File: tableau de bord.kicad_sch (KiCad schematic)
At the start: 19 parts, among them J2 Alim, SW1 LVMS, SW2 TS, SW3 R2D, SW4 TS OFF, SW5 SW_Push, U1 L7805

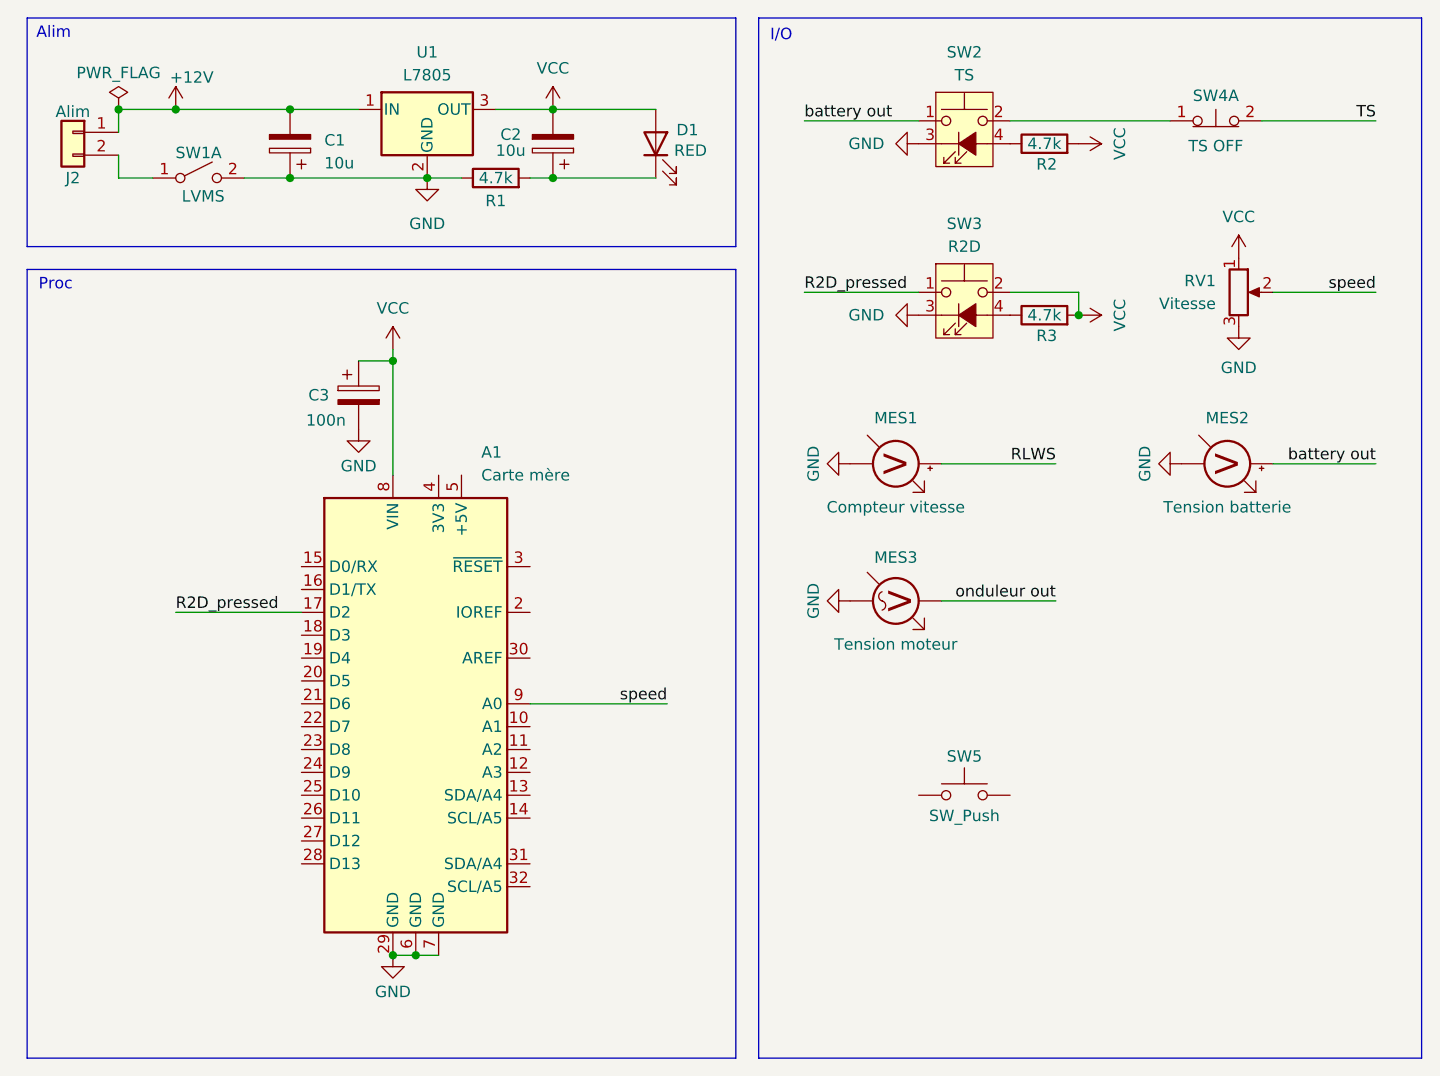
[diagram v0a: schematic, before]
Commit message: Ajout des boutons I/O pour les scénario et pannes
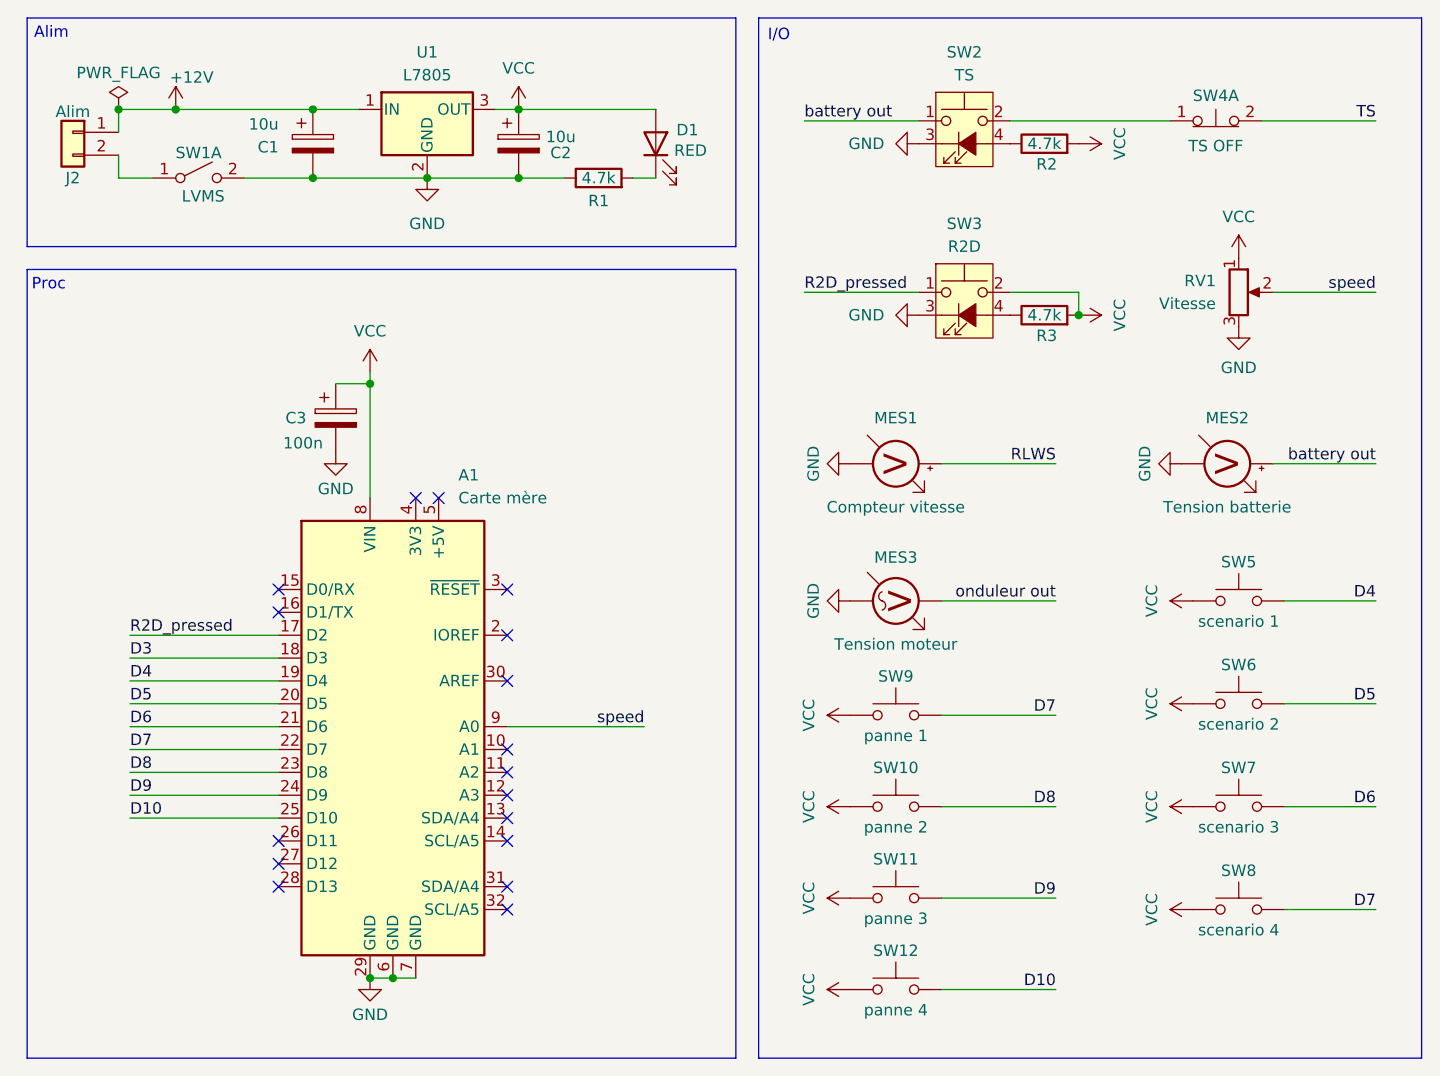
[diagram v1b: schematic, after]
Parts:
- added SW10: panne 2, symbol Switch:SW_Push
- added SW11: panne 3, symbol Switch:SW_Push
- added SW12: panne 4, symbol Switch:SW_Push
- added SW6: scenario 2, symbol Switch:SW_Push
- added SW7: scenario 3, symbol Switch:SW_Push
- added SW8: scenario 4, symbol Switch:SW_Push
- added SW9: panne 1, symbol Switch:SW_Push
- SW5: value SW_Push -> scenario 1
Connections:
- net +12V: now also C1.1; no longer C1.2
- net GND: now also C1.2, C2.2; no longer C1.1
- net VCC: now also C2.1, SW5.1, SW10.1, SW11.1, SW12.1, SW6.1, SW7.1, SW8.1, SW9.1; no longer C2.2
- net at D1.1 (K), R1.2: no longer C2.1
- net D3: now reaches A1.18 (D3)
- net D4: now reaches A1.19 (D4)
- net D4: now also SW5.2
- net D5: now reaches A1.20 (D5)
- net D5: now also SW6.2
- net D6: now reaches A1.21 (D6)
- net D6: now also SW7.2
- net D7: now reaches A1.22 (D7)
- net D7: now also SW8.2, SW9.2
- net D8: now reaches A1.23 (D8)
- net D8: now also SW10.2
- net D9: now reaches A1.24 (D9)
- net D9: now also SW11.2
- net D10: now reaches A1.25 (D10)
- net D10: now also SW12.2
- no-connect marks 0 -> 17
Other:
- moved on the sheet: A1, C1, C2, C3, SW5

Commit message: Retirer le voltmètre
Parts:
- removed MES1: Compteur vitesse, symbol Device:Voltmeter_DC
- removed MES2: Tension batterie, symbol Device:Voltmeter_DC
- removed MES3: Tension moteur, symbol Device:Voltmeter_AC
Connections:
- net D3: no longer names the net of A1.18 (D3)
- net battery out renamed +60V
- no-connect marks 17 -> 18
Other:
- moved on the sheet: SW10, SW11, SW12, SW5, SW6, SW7, SW8, SW9

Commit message: version prête pour révision
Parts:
- removed SW1: LVMS, symbol Switch:SW_DPST_x2
- removed SW4: TS OFF, symbol Switch:SW_Push_Open_Dual_x2
- added J1: Connecteur voiture, symbol Connector:Conn_01x02_Pin
- added SW1: LVMS, symbol Switch:SW_SPST
- added SW4: TSMS, symbol Switch:SW_Push_Open
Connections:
- net GND: now also SW1.2 (B)
- net TS: now also SW4.2 (B)
- net at A1.15 (D0/RX): now also J1.1 (Pin_1)
- net at A1.16 (D1/TX): now also J1.2 (Pin_2)
- net at SW2.2: now also SW4.1 (A)
- net at J2.2 (Pin_2): now also SW1.1 (A)
- no-connect marks 18 -> 16
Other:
- title: (none) -> Carte du tableu de bord

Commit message: Ajout de résistances pull up
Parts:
- removed SW8: scenario 4, symbol Switch:SW_Push
- added R10, R4, R5, R6, R7, R8, R9: 10k, symbol Device:R
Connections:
- net D10: now also R7.1
- net D4: now also R8.1
- net D5: now also R9.1
- net D6: now also R10.1
- net D7: now also R4.1
- net D8: now also R5.1
- net D9: now also R6.1
- net GND: now also SW10.1, SW11.1, SW12.1, SW5.1, SW6.1, SW7.1, SW9.1
- net VCC: now also R10.2, R4.2, R5.2, R6.2, R7.2, R8.2, R9.2; no longer SW10.1, SW11.1, SW12.1, SW5.1, SW6.1, SW7.1, SW9.1
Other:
- moved on the sheet: SW9

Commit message: Version 1
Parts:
- removed A1: Carte mère, Module:Arduino_UNO_R3, symbol MCU_Module:Arduino_UNO_R3
- removed C3: 100n, symbol Device:C_Polarized
- removed D1: RED, symbol Device:LED
- removed J1: Connecteur voiture, symbol Connector:Conn_01x02_Pin
- removed R1: 4.7k, symbol Device:R
- removed R10, R8, R9: 10k, symbol Device:R
- removed RV1: Vitesse, symbol Device:R_Potentiometer
- removed SW1: LVMS, symbol Switch:SW_SPST
- removed SW10: panne 2, symbol Switch:SW_Push
- removed SW11: panne 3, symbol Switch:SW_Push
- removed SW12: panne 4, symbol Switch:SW_Push
- removed SW2: TS, symbol Switch:SW_Push_LED
- removed SW3: R2D, symbol Switch:SW_Push_LED
- removed SW4: TSMS, symbol Switch:SW_Push_Open
- removed SW5: scenario 1, symbol Switch:SW_Push
- removed SW6: scenario 2, symbol Switch:SW_Push
- removed SW7: scenario 3, symbol Switch:SW_Push
- removed SW9: panne 1, symbol Switch:SW_Push
- added A2: Arduino_Nano_ESP32, Module:Arduino_Nano, symbol MCU_Module:Arduino_Nano_ESP32
- added J1: TS ON, Connector_PinSocket_2.00mm:PinSocket_1x03_P2.00mm_Vertical, symbol Connector:Conn_01x03_Socket
- added J3: R2D, Connector_PinSocket_2.00mm:PinSocket_1x03_P2.00mm_Vertical, symbol Connector:Conn_01x03_Socket
- added J4: Potentiometre, Connector_PinSocket_2.00mm:PinSocket_1x03_P2.00mm_Vertical, symbol Connector:Conn_01x03_Socket
- added J5: commande onduleur, Connector_PinSocket_2.00mm:PinSocket_1x02_P2.00mm_Vertical, symbol Connector:Conn_01x02_Socket
- C1, C2: footprint (none) -> Capacitor_THT:CP_Radial_D8.0mm_P5.00mm
- J2: footprint (none) -> Connector_PinSocket_2.00mm:PinSocket_1x02_P2.00mm_Vertical
- R2: footprint (none) -> Resistor_THT:R_Axial_DIN0204_L3.6mm_D1.6mm_P1.90mm_Vertical
- R3: value 4.7k -> 47k; footprint (none) -> Resistor_THT:R_Axial_DIN0204_L3.6mm_D1.6mm_P1.90mm_Vertical
- R4, R6, R7: value 10k -> 4.7k; footprint (none) -> Resistor_THT:R_Axial_DIN0204_L3.6mm_D1.6mm_P1.90mm_Vertical
- R5: value 10k -> 47k; footprint (none) -> Resistor_THT:R_Axial_DIN0204_L3.6mm_D1.6mm_P1.90mm_Vertical
- U1: footprint (none) -> Package_TO_SOT_THT:TO-220-3_Horizontal_TabDown
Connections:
- net D7 is gone; now on net GND: R4.1
- net GND: now also J2.2 (Pin_2), R2.1, A2.29 (GND), A2.4 (GND), J1.3 (Pin_3), J3.3 (Pin_3), J4.3 (Pin_3), J5.2 (Pin_2)
- net VCC: now also A2.30 (VIN), J4.1 (Pin_1); no longer R2.2, R3.2, R4.2, R5.2, R6.2, R7.2
- net at R3.1: now also R7.2
- net D10 renamed r2d
- net r2d: now also J3.2 (Pin_2)
- net D8: no longer names the net of R5.1
- net D8: now also R6.2
- net D9 renamed ts
- net ts: now also J1.2 (Pin_2)
- new net: A2.5 (D2), R4.2, R5.2
- new net: A2.7 (D4), R2.2, R3.2
- new net commande: A2.9 (D6), J5.1 (Pin_1)
- new net led r2d: A2.8 (D5), J3.1 (Pin_1)
- new net led ts: A2.6 (D3), J1.1 (Pin_1)
- new net vitesse: A2.19 (A0), J4.2 (Pin_2)
- no-connect marks 16 -> 21
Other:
- note removed: "I/O"

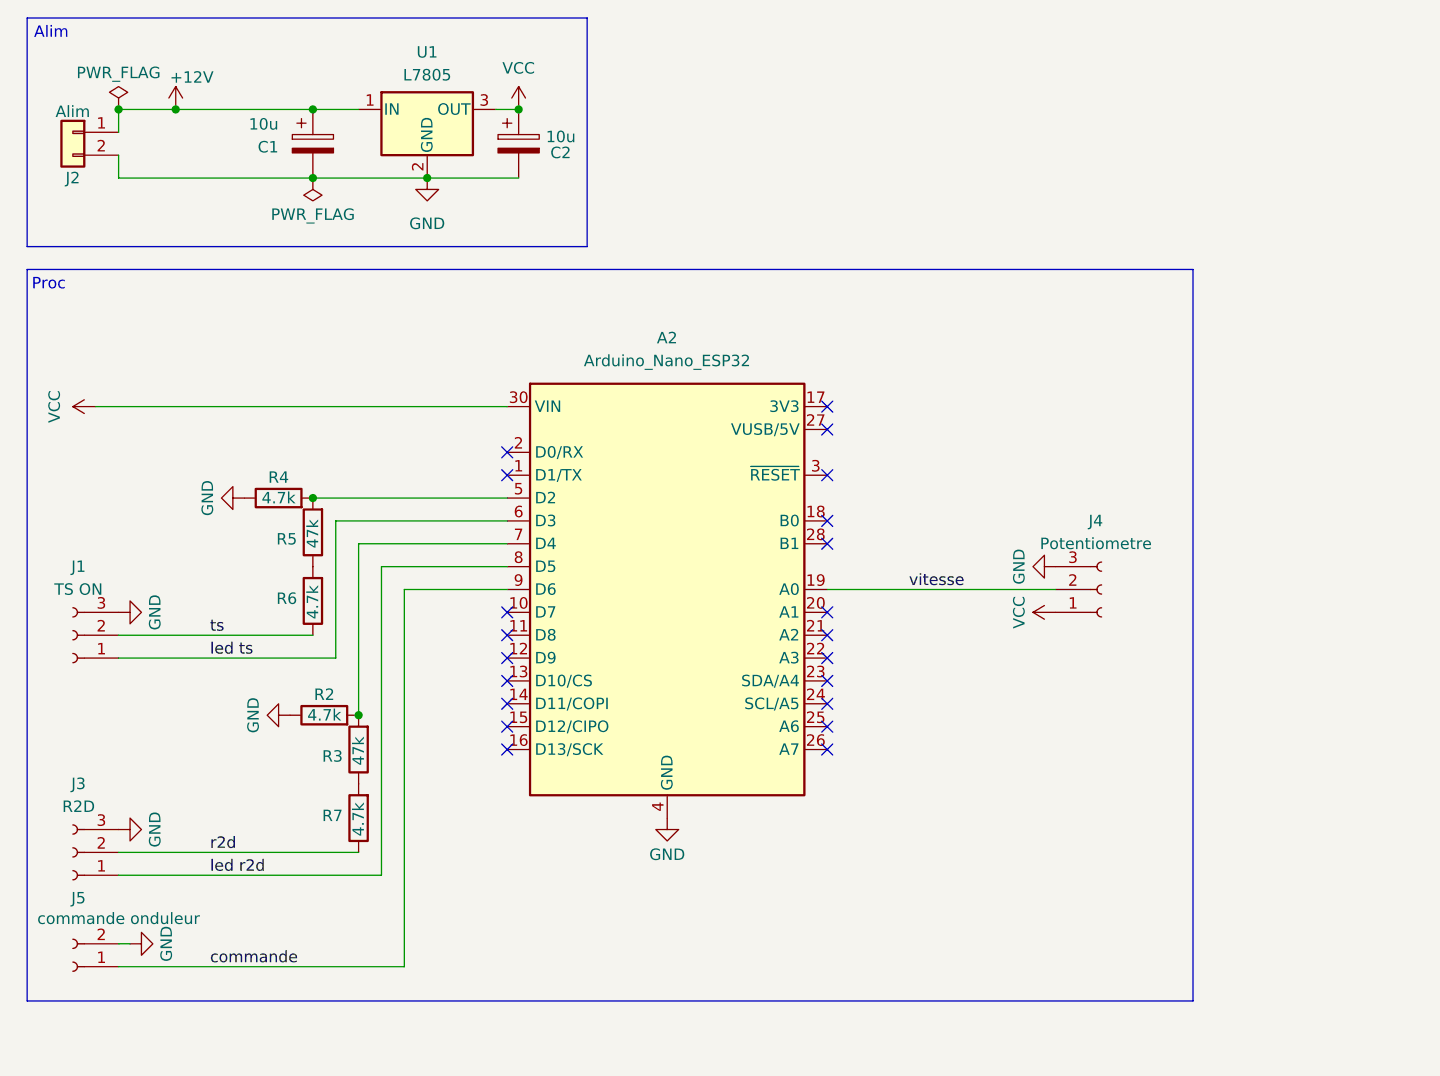
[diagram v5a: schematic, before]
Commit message: Version 2:
- ajout de mosfet pour commander les relais.
- mise en forme des connecteurs
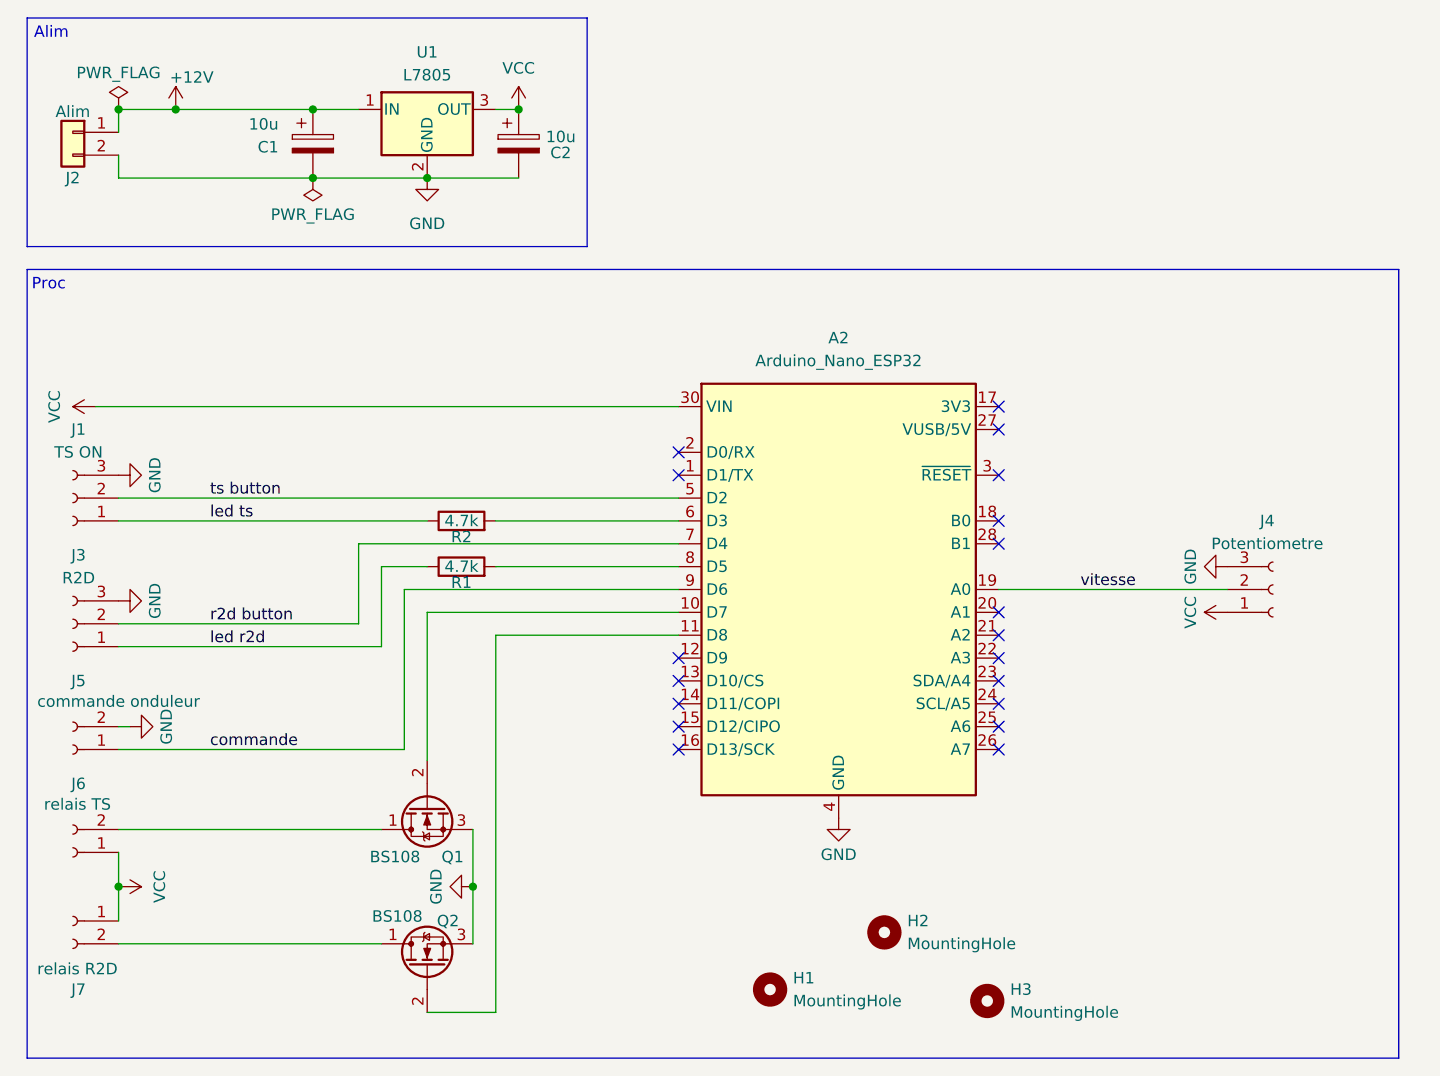
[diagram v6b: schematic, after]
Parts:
- removed R3, R5: 47k, Resistor_THT:R_Axial_DIN0204_L3.6mm_D1.6mm_P1.90mm_Vertical, symbol Device:R
- removed R4, R6, R7: 4.7k, Resistor_THT:R_Axial_DIN0204_L3.6mm_D1.6mm_P1.90mm_Vertical, symbol Device:R
- added H1, H2, H3: MountingHole, MountingHole:MountingHole_2.2mm_M2, symbol Mechanical:MountingHole
- added J6: relais TS, Connector_PinSocket_2.00mm:PinSocket_1x02_P2.00mm_Vertical, symbol Connector:Conn_01x02_Socket
- added J7: relais R2D, Connector_PinSocket_2.00mm:PinSocket_1x02_P2.00mm_Vertical, symbol Connector:Conn_01x02_Socket
- added Q1, Q2: BS108, Package_TO_SOT_THT:TO-92_Inline, symbol Transistor_FET:BS108
- added R1: 4.7k, Resistor_THT:R_Axial_DIN0204_L3.6mm_D1.6mm_P5.08mm_Horizontal, symbol Device:R
- C1, C2: footprint Capacitor_THT:CP_Radial_D8.0mm_P5.00mm -> Capacitor_THT:CP_Radial_D4.0mm_P1.50mm
- R2: footprint Resistor_THT:R_Axial_DIN0204_L3.6mm_D1.6mm_P1.90mm_Vertical -> Resistor_THT:R_Axial_DIN0204_L3.6mm_D1.6mm_P5.08mm_Horizontal
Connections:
- net ts is gone; now on net ts button: J1.2 (Pin_2)
- net GND: now also Q1.3 (S), Q2.3 (S); no longer R2.1
- net VCC: now also J6.1 (Pin_1), J7.1 (Pin_1)
- net led r2d: now also R1.1; no longer A2.8 (D5)
- net led ts: now also R2.1; no longer A2.6 (D3)
- net ts button: now reaches A2.5 (D2)
- net at A2.10 (D7): now also Q1.2 (G)
- net at A2.11 (D8): now also Q2.2 (G)
- net at R2.2: now also A2.6 (D3); no longer A2.7 (D4)
- net r2d renamed r2d button
- net r2d button: now also A2.7 (D4)
- new net: J7.2 (Pin_2), Q2.1 (D)
- new net: A2.8 (D5), R1.2
- new net: J6.2 (Pin_2), Q1.1 (D)
- no-connect marks 21 -> 19
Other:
- moved on the sheet: A2, J1, J3, J4, J5

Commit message: Nouveaux connecteurs, amélioration de la qualité
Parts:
- removed H1: MountingHole, MountingHole:MountingHole_2.2mm_M2, symbol Mechanical:MountingHole
- J1, J3, J4: footprint Connector_PinSocket_2.00mm:PinSocket_1x03_P2.00mm_Vertical -> Connector_JST:JST_XH_B3B-XH-A_1x03_P2.50mm_Vertical; symbol Connector:Conn_01x03_Socket -> Connector_Generic:Conn_01x03
- J2: footprint Connector_PinSocket_2.00mm:PinSocket_1x02_P2.00mm_Vertical -> Connector_JST:JST_XH_B2B-XH-A_1x02_P2.50mm_Vertical
- J5, J6, J7: footprint Connector_PinSocket_2.00mm:PinSocket_1x02_P2.00mm_Vertical -> Connector_JST:JST_XH_B2B-XH-A_1x02_P2.50mm_Vertical; symbol Connector:Conn_01x02_Socket -> Connector_Generic:Conn_01x02
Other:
- moved on the sheet: H3, J5, J6, J7
